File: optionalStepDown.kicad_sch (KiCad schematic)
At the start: 3 parts

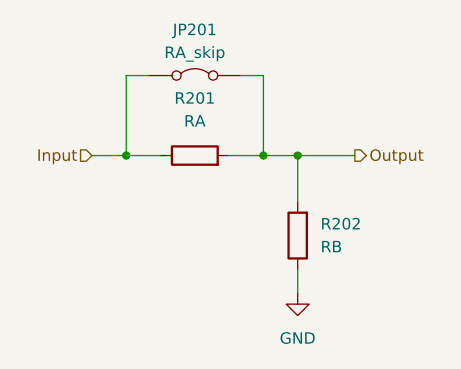
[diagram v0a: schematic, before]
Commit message: Final changes based on BoM
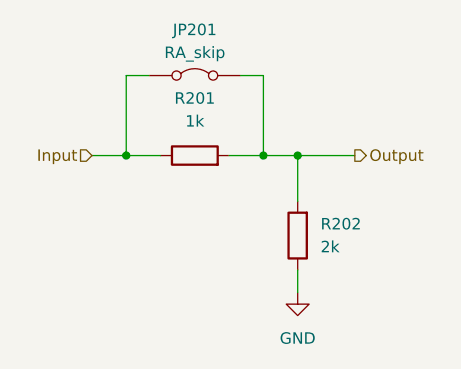
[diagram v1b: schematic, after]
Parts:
- R201: value RA -> 1k
- R202: value RB -> 2k
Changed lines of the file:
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@@
 			)
 		)
-		(property "Value" "RA"
+		(property "Value" "1k"
 			(at 120.65 102.87 90)
 			(show_name no)
@@
 			)
 		)
-		(property "Value" "RB"
+		(property "Value" "2k"
 			(at 134.62 116.8399 0)
 			(show_name no)
